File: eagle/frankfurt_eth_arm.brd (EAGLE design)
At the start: 72.2 x 65.5 mm, 85 parts, among them IC1 STM32F103C6T7A, IC2 ENC28J60-SO, IC3 SN65HVD232, IC4 LM2575S, IC5 11AA02E48, IC6 MCP23A256, IC7 AT45DB041D, J2 A00-108-220-450, Q1 8 MHz, Q2 25 MHz, X1 TAMPER, X2 32768 hZ

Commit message: Routed
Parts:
- removed JTAG: (no value), con-lstb:MA10-2
- removed R30, R31: 10K, rcl:R0805
- removed SJ1: (no value), jumper:SJ
- removed SV1, SV2: (no value), con-lstb:MA03-1
- added BOOT0, BOOT1: (no value), con-lstb:MA03-1
- added J1: (no value), con-lstb:MA05-2
- added J3: (no value), jumper:SJ
- added UART1: 22-23-2041, con-molex:22-23-2041
- R29: value 47K -> 10K
- R3: value 1K -> 10K
- moved R29 176.5 mm to (41.8, 43.9), turned to 90 degrees
- moved R24 147.7 mm to (39.4, 43.9), turned to 90 degrees
- moved R28 142.6 mm to (2.89, 25.4), turned to 90 degrees
- moved R23 139.6 mm to (55.3, 41.5), turned to 180 degrees
- moved C14 136.1 mm to (61.2, 43.8)
- moved X1 132.8 mm to (60.2, 39.1)
- moved R27 132.6 mm to (2.88, 21.2), turned to 90 degrees
- moved R26 122.0 mm to (2.92, 16.5), turned to 90 degrees
- moved R25 112.5 mm to (3.79, 12.7), turned to 180 degrees
- moved C20 103.9 mm to (27.4, 37.6), turned to 270 degrees
- moved X2 101.2 mm to (29.6, 38.2), turned to 270 degrees
- moved R22 98.8 mm to (19.0, 29.3), turned to 90 degrees
- moved C21 98.1 mm to (27.4, 33.5), turned to 90 degrees
- moved C19 90.5 mm to (33.1, 35.1)
- moved C18 88.3 mm to (40.7, 33.3), turned to 90 degrees
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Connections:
- net N$23 renamed BOOT0
- removed net INT0: IC2.4
- removed net INT1: IC2.5
- removed net N$18: R20.1, SV1.2
- removed net N$26: R21.1, SV2.2
- removed net N$30: IC1.32
- removed net N$31: IC1.33
- removed net N$32: JTAG.12, R31.2
- removed net N$36: JTAG.18, R30.2
- removed net N$38: JTAG.20, R29.2
- removed net N$4: R3.2
- removed net N$6: C7.2, R4.1, S1.1
- removed net REST: C5.1, IC1.7, R2.1
- removed net SWCK: IC1.37
- removed net SWDIO: IC1.34
- removed net SWO: IC1.39
- removed net TCK: JTAG.10, R27.1
- removed net TDO: JTAG.14, R28.1
- removed net TMS: JTAG.8, R26.1
- removed net VREF: IC3.5
- new net CANRXD: IC1.32, IC3.4
- new net CANTXD: IC1.33, IC3.1
- new net ETH_INT0: IC1.45, IC2.4, R24.2
- new net ETH_INT1: IC1.46, IC2.5, R29.2
- new net INIT: IC1.26, R3.2
- new net INITSW: C7.2, IC1.27, R4.1, S1.1
- new net SWDIO/TMS: IC1.34, J1.2, R25.1
- new net TCK/SWCK: IC1.37, J1.4, R26.1
- new net TDO/SWO: IC1.39, J1.6, R27.1
- new net UART1_RX: IC1.31, UART1.2
- new net UART1_TX: IC1.30, UART1.3
- new net _BOOT0: BOOT0.2, R20.1
- new net _BOOT1: BOOT1.2, R21.1
- net CANL: now also IC3.5
- net ETH_CS: now also IC1.14
- net ETH_RESET: now also IC1.28
- net EUI48: now also IC1.22
- net GND: now also BOOT0.1, BOOT1.1, J1.3, J1.5, J1.7, J1.9, UART1.4; no longer JTAG.11, JTAG.13, JTAG.15, JTAG.17, JTAG.19, JTAG.3, JTAG.5, JTAG.7, JTAG.9, R29.1, R30.1, R31.1, SV1.1, SV2.1
- net MISO: now also IC1.16
- net MOSI: now also IC1.17
- net RAM_CS: now also IC1.21
- net ROM_CS1: now also IC1.13
- net RST: now also C5.1, IC1.7, J3.2, R2.1; no longer JTAG.16, SJ1.2
- net SCK: now also IC1.15
- net TDI: now also J1.8, R28.1; no longer JTAG.6, R25.1
- net TRST: now also J1.10, J3.1; no longer JTAG.4, R24.1, SJ1.1
- net VCC: now also BOOT0.3, BOOT1.3, J1.1, R24.1, R29.1, UART1.1; no longer JTAG.1, JTAG.2, R24.2, SV1.3, SV2.3
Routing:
- net VCC: track 302.5 -> 530.4 mm, vias 3 -> 5
- net MOSI: track 0.00 -> 109.6 mm, vias 0 -> 6
- net SCK: track 0.00 -> 101.1 mm, vias 0 -> 6
- net MISO: track 0.00 -> 93.3 mm, vias 0 -> 5
- net EUI48: track 2.38 -> 77.7 mm, vias 0 -> 2
- net SWDIO/TMS: track 0.00 -> 66.2 mm, vias 0 -> 2
- net TCK/SWCK: track 0.00 -> 62.6 mm, vias 0 -> 1
- net TDO/SWO: track 0.00 -> 56.1 mm, vias 0 -> 2
- net N$27: track 0.00 -> 52.8 mm, vias 0 -> 1
- net TRST: track 0.00 -> 49.1 mm, vias 0 -> 1
- net BOOT0: track 0.00 -> 46.5 mm, vias 0 -> 2
- net ETH_CS: track 3.65 -> 49.6 mm, vias 0 -> 2
- net TDI: track 0.00 -> 45.2 mm, vias 0 -> 4
- net INITSW: track 0.00 -> 43.8 mm, vias 0 -> 2
- net BOOT1: track 0.00 -> 42.6 mm, vias 0 -> 2
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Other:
- board text added: "CON"
- board text added: "OFF"
- board text added: "WRN"

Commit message: Clean
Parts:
- moved U$2 51.4 mm to (57.5, 29.0)
- moved R28 11.1 mm to (11.9, 18.9), turned to 270 degrees
- moved C6 0.72 mm to (28.6, 21.5)
- moved C4 0.59 mm to (27.8, 42.2)
- moved X2 0.22 mm to (29.3, 38.1)
- moved R7 0.20 mm to (52.1, 44.0)
- moved R23 0.18 mm to (55.3, 41.3)
- moved R27 0.12 mm to (2.76, 21.2)
- moved R6 0.12 mm to (47.1, 43.5)
- moved D1 0.09 mm to (67.1, 12.3)
- moved C5 0.06 mm to (19.0, 24.9)
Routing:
- net TDO/SWO: track 56.1 -> 104.0 mm, vias 2 -> 4
- net GND: track 87.7 -> 104.1 mm, vias 26 -> 32
- net VCC: track 530.4 -> 545.9 mm
- net N$7: track 13.8 -> 23.6 mm, vias 0 -> 2
- net CANRXD: track 19.4 -> 25.1 mm
- net MOSI: track 109.6 -> 105.7 mm
- net N$10: track 19.3 -> 23.1 mm
- net RST: track 26.8 -> 29.7 mm
- net TDI: track 45.2 -> 43.5 mm
- net ROM_CS1: track 37.5 -> 36.3 mm
- net INITSW: track 43.8 -> 44.8 mm
- net N$2: track 24.9 -> 25.8 mm
- net _BOOT1: track 6.85 -> 7.63 mm
- net MISO: track 93.3 -> 93.9 mm
- net SWDIO/TMS: track 66.2 -> 66.8 mm, vias 2 -> 1
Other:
- board text added: "Frankfurt Eth"
- board text removed: "Frankfurt Ethernet"

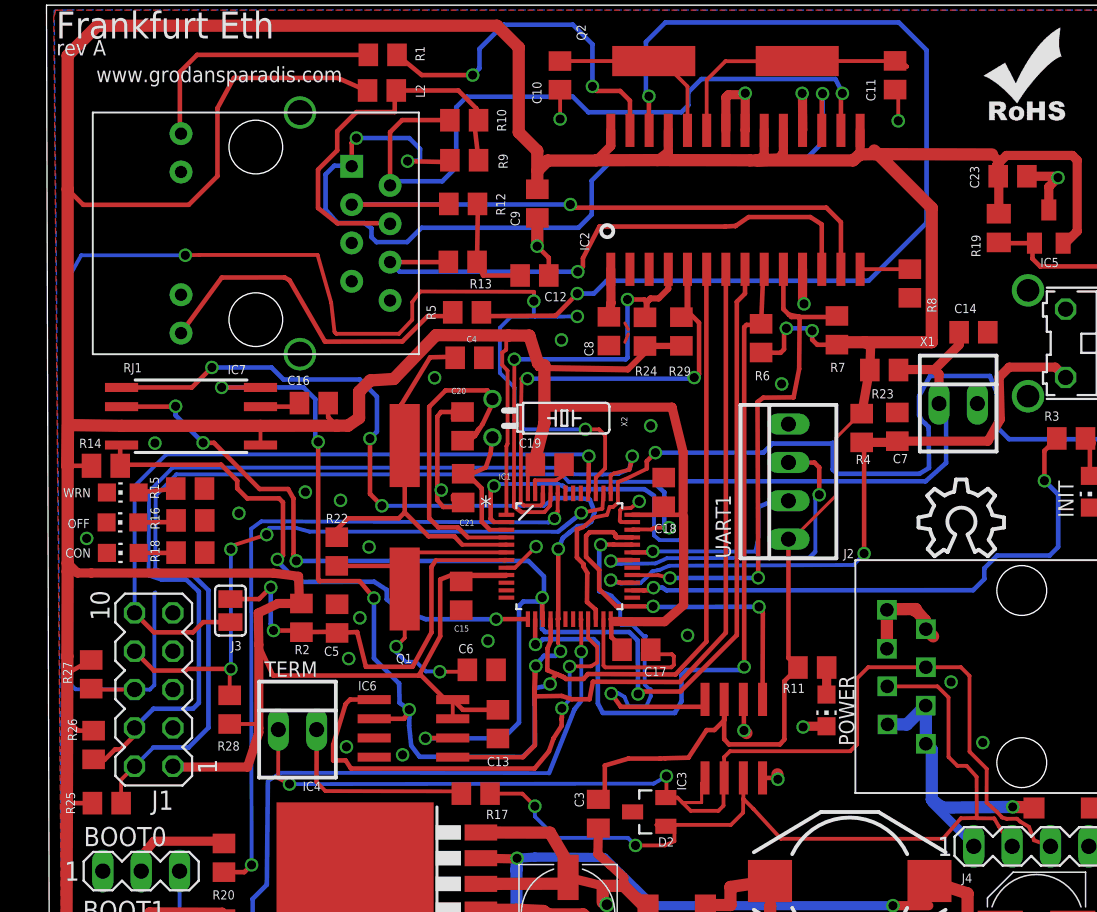
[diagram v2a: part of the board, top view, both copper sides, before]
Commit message: Removed extra status LED's
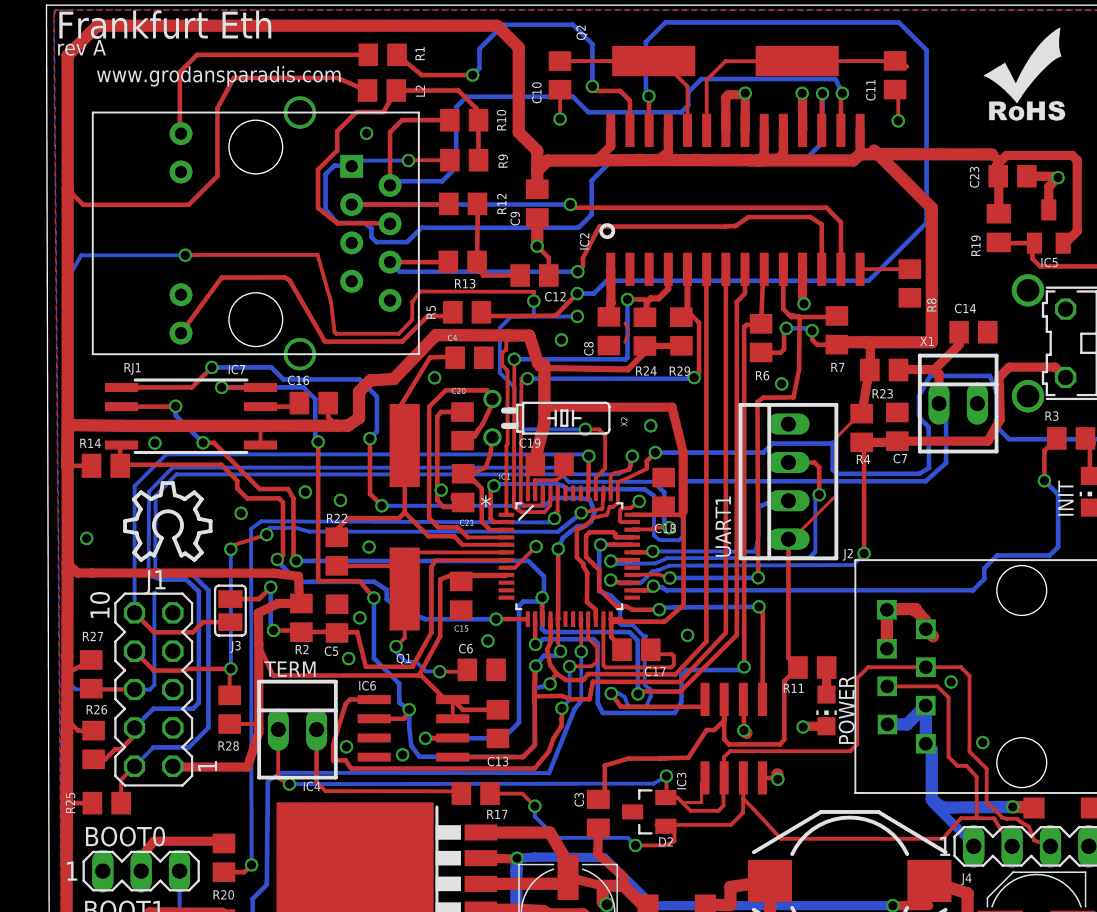
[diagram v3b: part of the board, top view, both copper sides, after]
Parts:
- removed LED3, LED4, LED5: (no value), led:CHIP-LED0805
- removed R15, R16, R18: 1K, rcl:R0805
- moved U$2 52.5 mm to (5.00, 28.8)
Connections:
- removed net LED_BUS_OFF: R18.2
- removed net LED_CONNECTED: R15.2
- removed net N$14: LED3.A, R15.1
- removed net N$21: LED4.A, R16.1
- removed net N$24: LED5.A, R18.1
- net GND: no longer LED3.C, LED4.C, LED5.C
- net LED_BUS_WARN: now also IC1.25; no longer R16.2
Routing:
- net TPOUT+: track 59.1 -> 54.8 mm, vias 3 -> 2
- net N$21: track 2.52 -> 0.00 mm
- net N$24: track 2.48 -> 0.00 mm
- net N$14: track 2.47 -> 0.00 mm
- net N$19: track 26.7 -> 25.9 mm
- net MISO: track 93.9 -> 93.3 mm
- net GND: vias 32 -> 33
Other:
- board text removed: "CON"
- board text removed: "OFF"
- board text removed: "WRN"

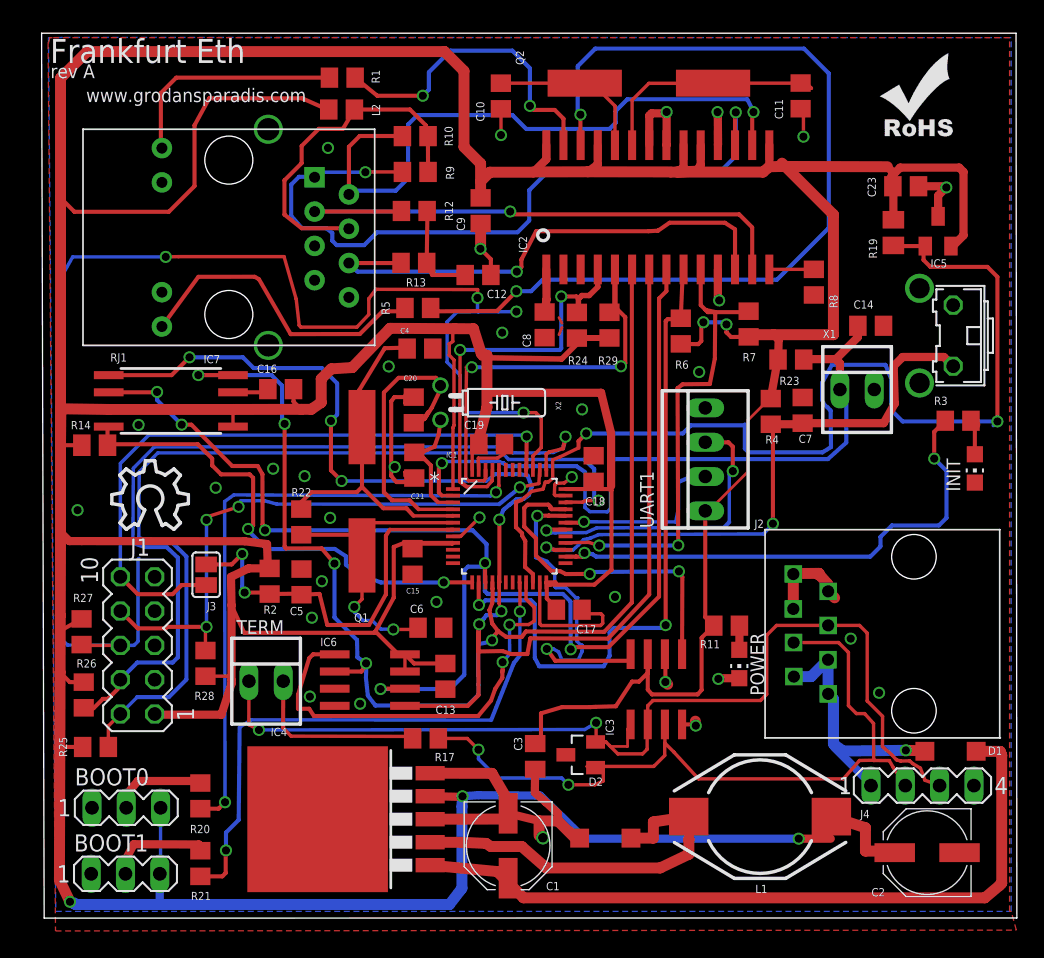
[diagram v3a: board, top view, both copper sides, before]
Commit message: edit text layer
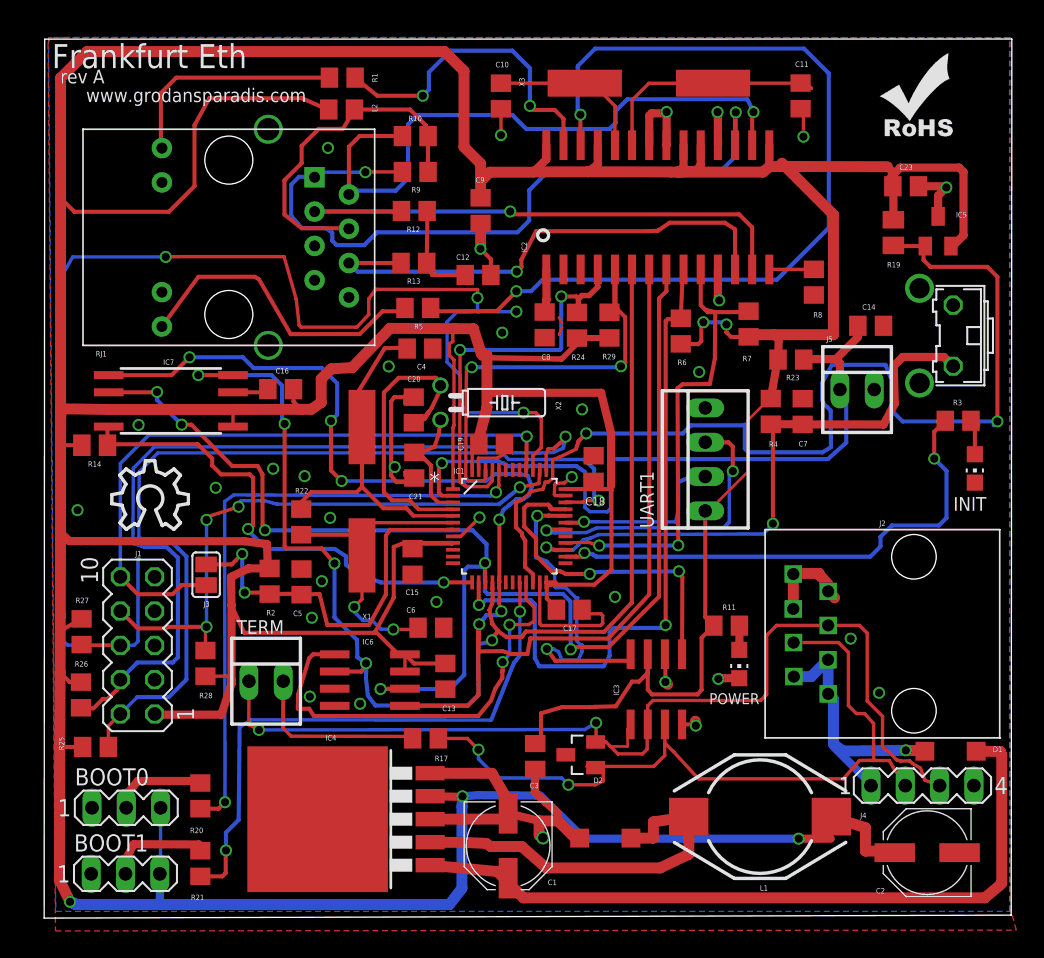
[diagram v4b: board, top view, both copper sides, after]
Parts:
- removed Q1: 8 MHz, vscpcan:9C
- added J5: TAMPER, con-molex:22-23-2021
- X1: value TAMPER -> 8 MHz; device con-molex:22-23-2021 -> vscpcan:9C
- moved X1 37.4 mm to (23.5, 31.6), turned to 270 degrees
- moved R26 0.21 mm to (2.71, 16.5)
- moved C7 0.09 mm to (56.1, 37.5)
- renumbered Q2 to X3
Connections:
- net GND: now also J5.2; no longer X1.2
- net N$2: now also X1.P$1; no longer Q1.P$1
- net N$27: now also J5.1; no longer X1.1
- net N$7: now also X1.P$2; no longer Q1.P$2
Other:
- board size 72.2 x 65.5 mm -> 71.6 x 65.1 mm

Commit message: Added Gerbers
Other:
- board size 71.6 x 65.1 mm -> 71.7 x 65.1 mm
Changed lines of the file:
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@@
 <text x="69.74" y="31.16" size="1.016" layer="25" rot="R180">INIT</text>
 <wire x1="-0.01" y1="-0.01" x2="0.03" y2="65.06" width="0" layer="20"/>
-<wire x1="0.03" y1="65.06" x2="71.63" y2="65.07" width="0" layer="20"/>
-<wire x1="71.63" y1="65.07" x2="71.58" y2="0.21" width="0" layer="20"/>
-<wire x1="71.58" y1="0.21" x2="-0.01" y2="-0.01" width="0" layer="20"/>
+<wire x1="0.03" y1="65.06" x2="71.51" y2="65.07" width="0" layer="20"/>
+<wire x1="71.51" y1="65.07" x2="71.64" y2="0.02" width="0" layer="20"/>
+<wire x1="71.64" y1="0.02" x2="-0.01" y2="-0.01" width="0" layer="20"/>
 <circle x="36.93" y="50.54" radius="0.1220625" width="0.8128" layer="25"/>
 </plain>

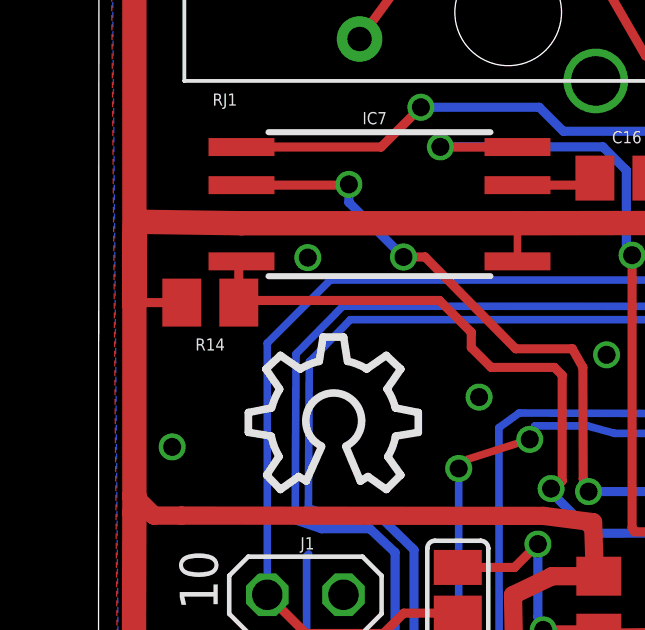
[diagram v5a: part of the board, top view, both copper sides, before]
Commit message: Moved out R14 a bit
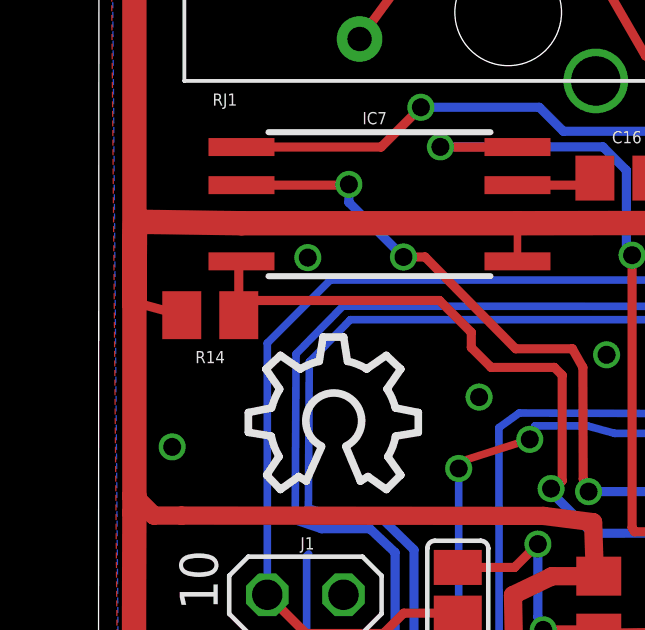
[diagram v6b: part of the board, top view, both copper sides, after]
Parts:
- moved R14 0.42 mm to (3.73, 34.6)
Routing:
- net ROM_CS1: track 36.3 -> 37.1 mm
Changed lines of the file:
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@@
 <attribute name="NAME" x="8.8" y="40.945" size="0.4064" layer="25"/>
 </element>
-<element name="R14" library="rcl" package="M0805" value="100k" x="3.73" y="35" smashed="yes" rot="R180">
-<attribute name="NAME" x="3.23" y="33.4" size="0.4064" layer="25"/>
+<element name="R14" library="rcl" package="M0805" value="100k" x="3.73" y="34.58" smashed="yes" rot="R180">
+<attribute name="NAME" x="3.23" y="32.98" size="0.4064" layer="25"/>
 </element>
 <element name="C16" library="rcl" package="C0805" value="0.1uF" x="17.5" y="39.15" smashed="yes">
@@
 <wire x1="48.66" y1="16.88" x2="48.66" y2="20.74" width="0.3048" layer="1"/>
 <wire x1="48.66" y1="20.74" x2="49.56" y2="21.64" width="0.3048" layer="1"/>
-<wire x1="2.78" y1="35" x2="1.24" y2="35" width="0.3048" layer="1"/>
+<wire x1="2.78" y1="34.58" x2="1.24" y2="35" width="0.3048" layer="1"/>
 <wire x1="1.24" y1="35" x2="1.2" y2="34.96" width="0.3048" layer="1"/>
 <wire x1="18.45" y1="39.15" x2="18.45" y2="38.224640625" width="0.3048" layer="1"/>
@@
 <contactref element="IC7" pad="4"/>
 <contactref element="R14" pad="1"/>
-<wire x1="4.68" y1="35" x2="4.68" y2="36.285" width="0.3048" layer="1"/>
+<wire x1="4.68" y1="34.58" x2="4.68" y2="36.285" width="0.3048" layer="1"/>
 <wire x1="4.68" y1="36.285" x2="4.77" y2="36.375" width="0.3048" layer="1"/>
 <contactref element="IC1" pad="13"/>
@@
 <wire x1="12.43" y1="34.01" x2="11.37" y2="35.07" width="0.3048" layer="1"/>
 <wire x1="11.37" y1="35.07" x2="4.75" y2="35.07" width="0.3048" layer="1"/>
-<wire x1="4.75" y1="35.07" x2="4.68" y2="35" width="0.3048" layer="1"/>
+<wire x1="4.75" y1="35.07" x2="4.68" y2="34.58" width="0.3048" layer="1"/>
 </signal>
 <signal name="BOOT0">
